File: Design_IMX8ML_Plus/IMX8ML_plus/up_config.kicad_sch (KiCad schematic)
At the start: 31 parts, among them U1 MIMX8ML8CVNKZAB, U6 KSZ9131RNXI, Y3 24MHz, Y4 25MHz

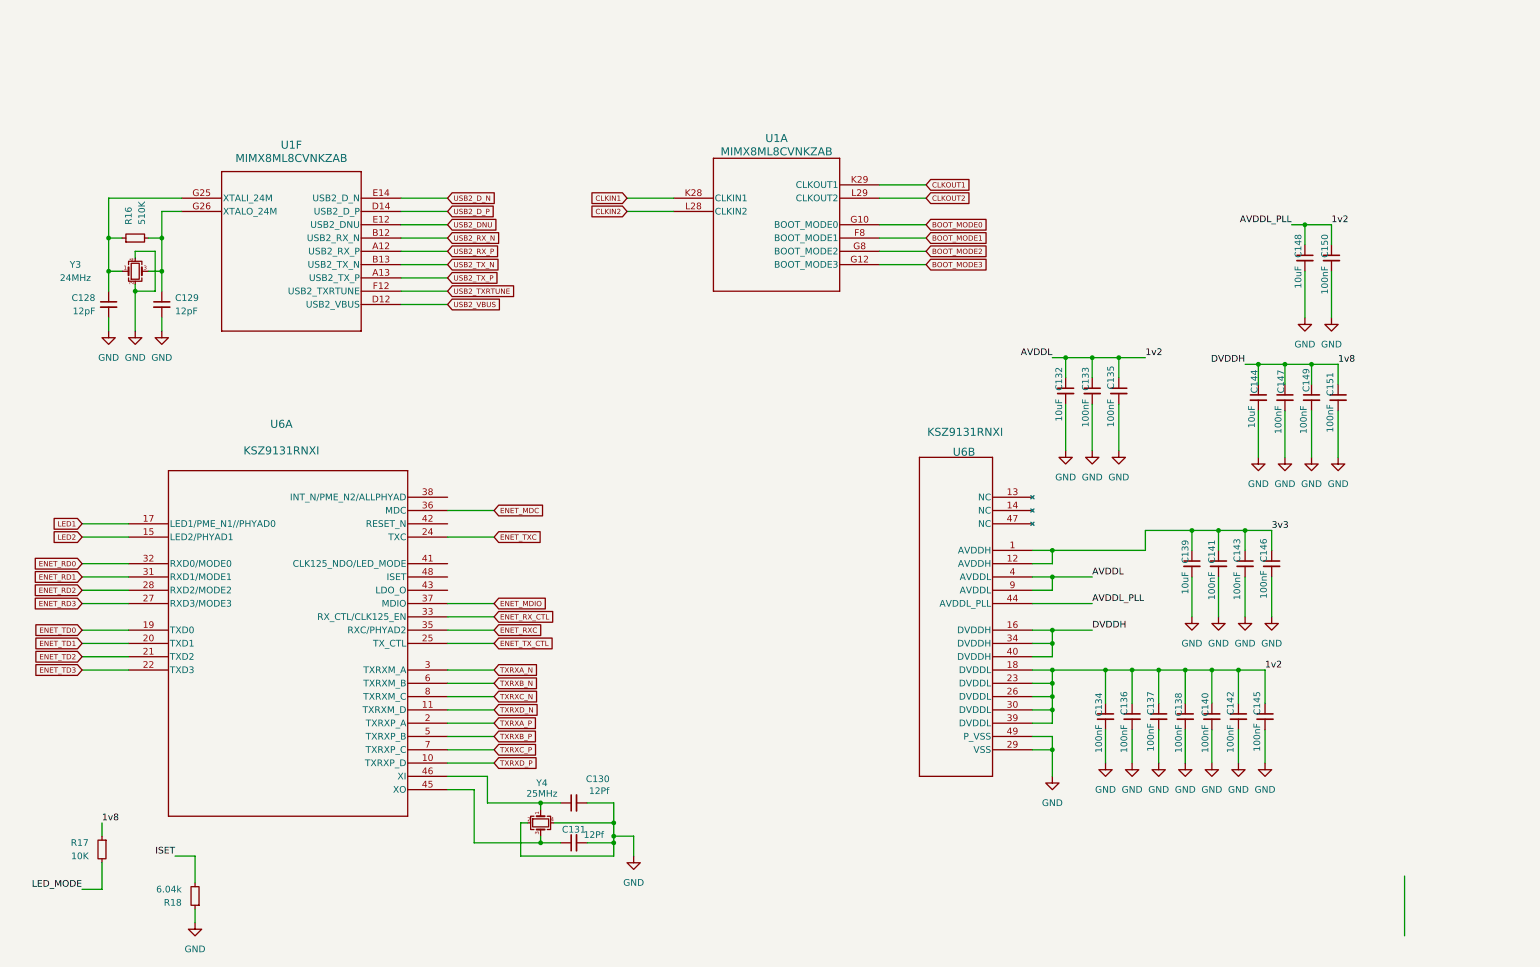
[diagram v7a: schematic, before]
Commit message: [CPU/BB] Improving the conection between the cpu and BB
* Reorganization of the components in the Base board.
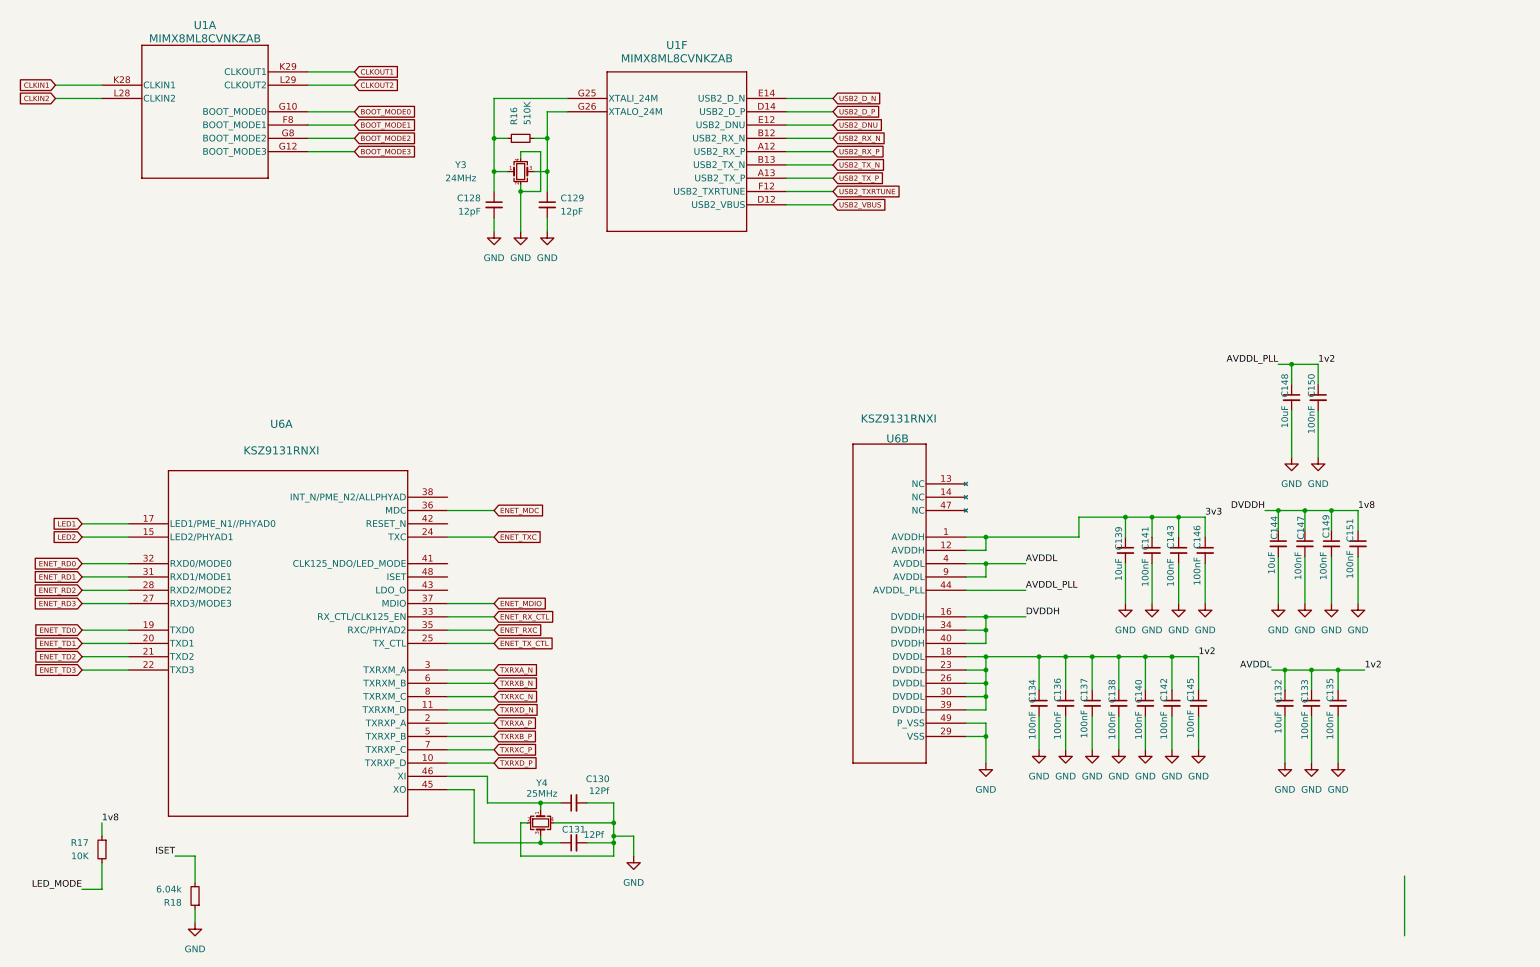
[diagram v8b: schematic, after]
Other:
- moved on the sheet: C128, C129, C132, C133, C134, C135, C136, C137, C138, C139, C140, C141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
